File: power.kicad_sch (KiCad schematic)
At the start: 71 parts, among them J2 Molex_Mini-Fit_2x3_50362462, Q16 DMG1012T-7, Q2 SISS05DN-T1-GE3, Q23 SISS05DN-T1-GE3, Q24 SISS05DN-T1-GE3, Q25 SISS05DN-T1-GE3, Q39 SISS05DN-T1-GE3, Q4 DMG1012T-7, Q5 SISS05DN-T1-GE3, Q6 DMG1012T-7, Q9 SISS05DN-T1-GE3, U15 NCP718BSN330T1G, U6 LTC4412IS6, U61 LTC4412IS6, U62 LTC4412IS6, U63 LTC4412IS6, U64 LTC4412IS6

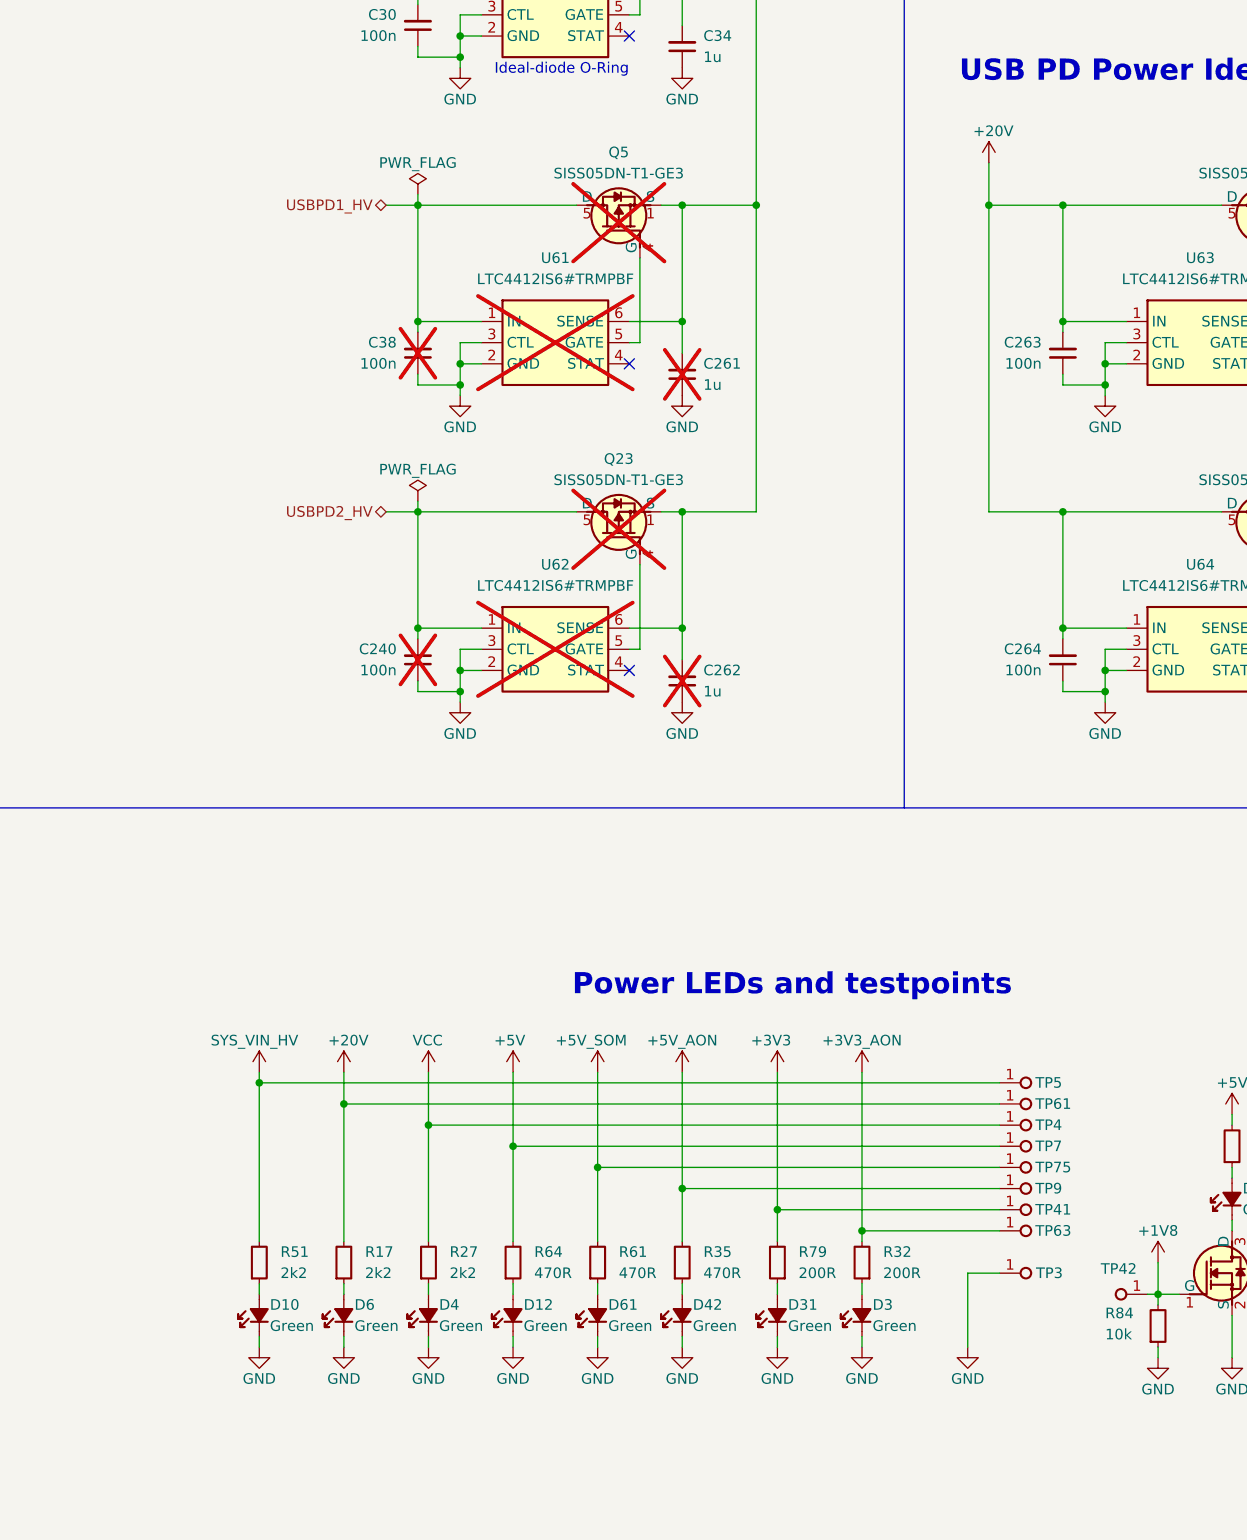
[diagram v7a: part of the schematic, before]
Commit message: [#85326] Add SoM capacitors, add testpoints
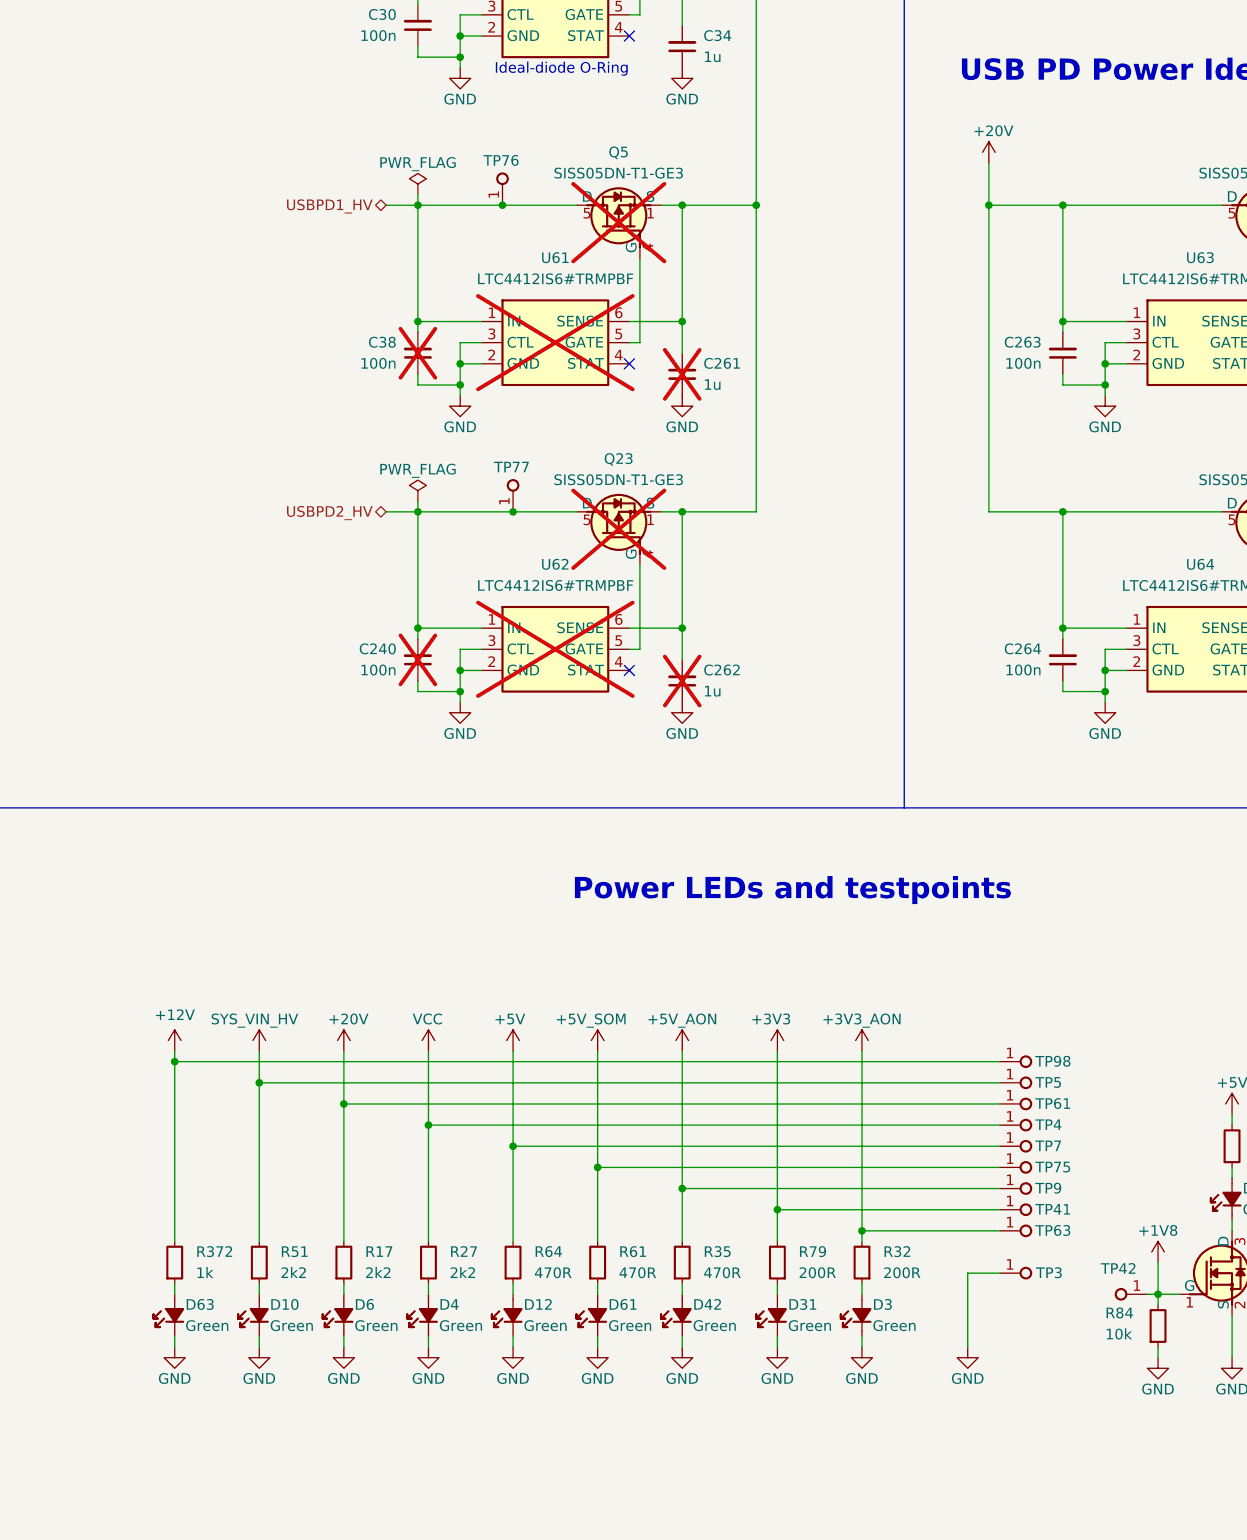
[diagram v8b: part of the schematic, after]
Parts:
- added D63: LED_G_0603_LTST-C190GKT, antmicro-footprints:LED_0603_1608Metric_G, symbol antmicroLEDIndicationDiscrete:LED_G_0603_LTST-C190GKT
- added R372: R_1k_0402, antmicro-footprints:R_0402_1005Metric, symbol antmicroResistors0402:R_1k_0402
- added TP76, TP77, TP98: TP_0.75mm_SMD, antmicro-footprints:TP_SMD_0.75mm, symbol antmicroTestPoints:TP_0.75mm_SMD
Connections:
- net GND: now also D63.1 (C)
- net USBPD1_HV: now also TP76.1
- net USBPD2_HV: now also TP77.1
- new net: D63.2 (A), R372.1
- new net +12V: R372.2, TP98.1
